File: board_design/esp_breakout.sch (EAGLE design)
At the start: 14 parts, among them J3 USB_MINI-B_SMT

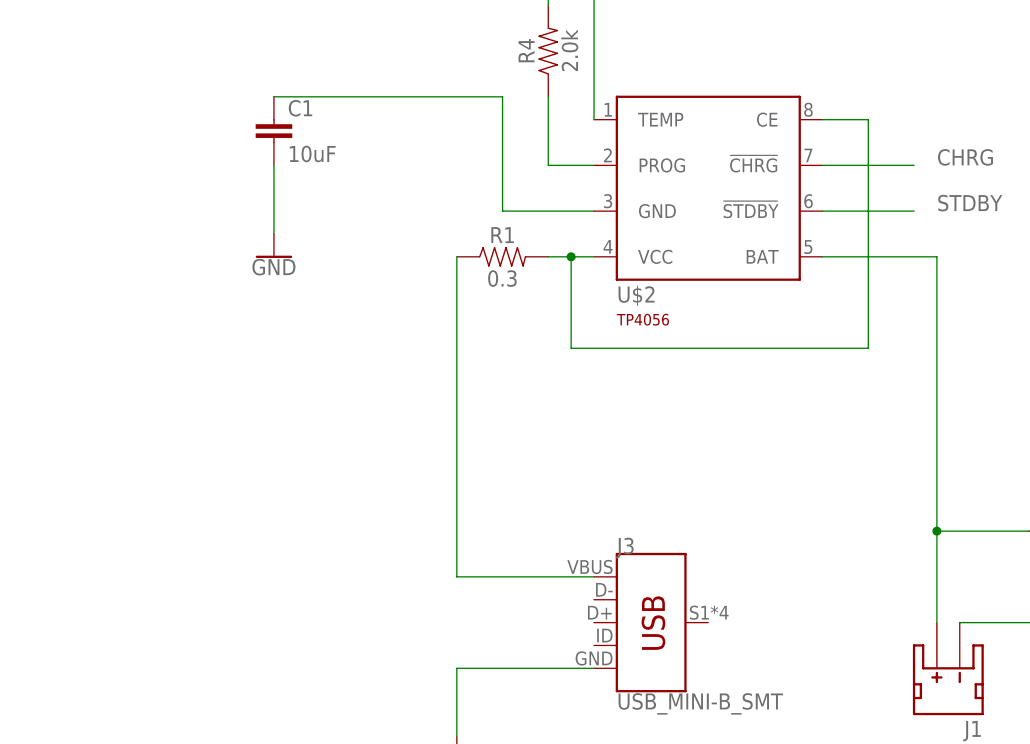
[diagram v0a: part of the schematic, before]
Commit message: upaded board to include 3.3v stepdown
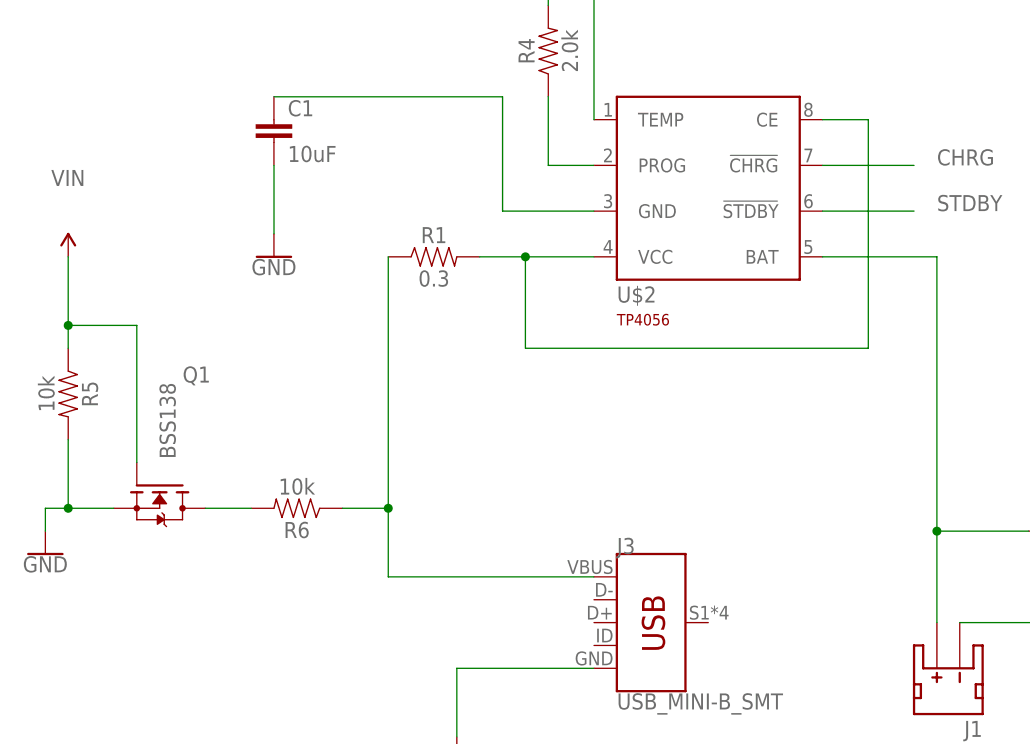
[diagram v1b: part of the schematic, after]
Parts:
- added Q1: BSS138, bss138_10:BSS138
- added R5, R6: 10k, SparkFun-Resistors:10KOHM-0603-1/10W-1%
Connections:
- new net N$10: Q1.D, R6.2
- net GND: now also Q1.S, R5.2
- net N$2: now also R6.1
- net VIN: now also Q1.G, R5.1
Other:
- moved on the sheet: R1
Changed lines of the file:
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@@
 <part name="C2" library="SparkFun-Capacitors" library_urn="urn:adsk.eagle:library:510" deviceset="10UF" device="-0805-10V-10%" package3d_urn="urn:adsk.eagle:package:37429/1" value="10uF"/>
 <part name="GND9" library="SparkFun-PowerSymbols" library_urn="urn:adsk.eagle:library:530" deviceset="GND" device=""/>
+<part name="Q1" library="bss138_10" deviceset="BSS138" device=""/>
+<part name="R6" library="SparkFun-Resistors" library_urn="urn:adsk.eagle:library:532" deviceset="10KOHM" device="-0603-1/10W-1%" package3d_urn="urn:adsk.eagle:package:39650/1" value="10k"/>
+<part name="R5" library="SparkFun-Resistors" library_urn="urn:adsk.eagle:library:532" deviceset="10KOHM" device="-0603-1/10W-1%" package3d_urn="urn:adsk.eagle:package:39650/1" value="10k"/>
+<part name="SUPPLY4" library="SparkFun-PowerSymbols" library_urn="urn:adsk.eagle:library:530" deviceset="VIN" device=""/>
+<part name="GND10" library="SparkFun-PowerSymbols" library_urn="urn:adsk.eagle:library:530" deviceset="GND" device=""/>
 </parts>
 <sheets>
@@
 <attribute name="NAME" x="-55.88" y="-48.26" size="1.778" layer="95" font="vector"/>
 </instance>
-<instance part="R1" gate="G$1" x="-68.58" y="-15.24" smashed="yes">
-<attribute name="NAME" x="-68.58" y="-13.716" size="1.778" layer="95" font="vector" align="bottom-center"/>
-<attribute name="VALUE" x="-68.58" y="-16.764" size="1.778" layer="96" font="vector" align="top-center"/>
+<instance part="R1" gate="G$1" x="-76.2" y="-15.24" smashed="yes">
+<attribute name="NAME" x="-76.2" y="-13.716" size="1.778" layer="95" font="vector" align="bottom-center"/>
+<attribute name="VALUE" x="-76.2" y="-16.764" size="1.778" layer="96" font="vector" align="top-center"/>
 </instance>
 <instance part="GND7" gate="1" x="-93.98" y="-15.24" smashed="yes">
@@
 <instance part="GND9" gate="1" x="7.62" y="-66.04" smashed="yes">
 <attribute name="VALUE" x="7.62" y="-66.294" size="1.778" layer="96" align="top-center"/>
+</instance>
+<instance part="Q1" gate="G$1" x="-106.68" y="-40.64" smashed="yes" rot="R270">
+<attribute name="VALUE" x="-106.68" y="-29.21" size="1.778" layer="96" rot="R270"/>
+<attribute name="NAME" x="-104.14" y="-29.21" size="1.778" layer="95"/>
+</instance>
+<instance part="R6" gate="G$1" x="-91.44" y="-43.18" smashed="yes" rot="R180">
+<attribute name="NAME" x="-91.44" y="-44.704" size="1.778" layer="95" font="vector" rot="R180" align="bottom-center"/>
+<attribute name="VALUE" x="-91.44" y="-41.656" size="1.778" layer="96" font="vector" rot="R180" align="top-center"/>
+</instance>
+<instance part="R5" gate="G$1" x="-116.84" y="-30.48" smashed="yes" rot="R270">
+<attribute name="NAME" x="-115.316" y="-30.48" size="1.778" layer="95" font="vector" rot="R270" align="bottom-center"/>
+<attribute name="VALUE" x="-118.364" y="-30.48" size="1.778" layer="96" font="vector" rot="R270" align="top-center"/>
+</instance>
+<instance part="SUPPLY4" gate="G$1" x="-116.84" y="-15.24" smashed="yes">
+<attribute name="VALUE" x="-116.84" y="-7.366" size="1.778" layer="96" align="bottom-center"/>
+</instance>
+<instance part="GND10" gate="1" x="-119.38" y="-48.26" smashed="yes">
+<attribute name="VALUE" x="-119.38" y="-48.514" size="1.778" layer="96" align="top-center"/>
 </instance>
 </instances>
@@
 <junction x="7.62" y="-55.88"/>
 </segment>
+<segment>
+<pinref part="Q1" gate="G$1" pin="S"/>
+<wire x1="-111.76" y1="-43.18" x2="-116.84" y2="-43.18" width="0.1524" layer="91"/>
+<pinref part="GND10" gate="1" pin="GND"/>
+<wire x1="-116.84" y1="-43.18" x2="-119.38" y2="-43.18" width="0.1524" layer="91"/>
+<wire x1="-119.38" y1="-43.18" x2="-119.38" y2="-45.72" width="0.1524" layer="91"/>
+<pinref part="R5" gate="G$1" pin="2"/>
+<wire x1="-116.84" y1="-35.56" x2="-116.84" y2="-43.18" width="0.1524" layer="91"/>
+<junction x="-116.84" y="-43.18"/>
+</segment>
 </net>
 <net name="N$1" class="0">
@@
 <pinref part="SUPPLY2" gate="G$1" pin="VIN"/>
 </segment>
+<segment>
+<pinref part="Q1" gate="G$1" pin="G"/>
+<wire x1="-109.22" y1="-38.1" x2="-109.22" y2="-22.86" width="0.1524" layer="91"/>
+<wire x1="-109.22" y1="-22.86" x2="-116.84" y2="-22.86" width="0.1524" layer="91"/>
+<pinref part="R5" gate="G$1" pin="1"/>
+<wire x1="-116.84" y1="-22.86" x2="-116.84" y2="-25.4" width="0.1524" layer="91"/>
+<pinref part="SUPPLY4" gate="G$1" pin="VIN"/>
+<wire x1="-116.84" y1="-15.24" x2="-116.84" y2="-22.86" width="0.1524" layer="91"/>
+<junction x="-116.84" y="-22.86"/>
+</segment>
 </net>
 <net name="N$2" class="0">
@@
 <pinref part="R1" gate="G$1" pin="1"/>
 <pinref part="J3" gate="G$1" pin="VBUS"/>
-<wire x1="-73.66" y1="-15.24" x2="-73.66" y2="-50.8" width="0.1524" layer="91"/>
-<wire x1="-73.66" y1="-50.8" x2="-58.42" y2="-50.8" width="0.1524" layer="91"/>
+<wire x1="-81.28" y1="-15.24" x2="-81.28" y2="-43.18" width="0.1524" layer="91"/>
+<wire x1="-81.28" y1="-43.18" x2="-81.28" y2="-50.8" width="0.1524" layer="91"/>
+<wire x1="-81.28" y1="-50.8" x2="-58.42" y2="-50.8" width="0.1524" layer="91"/>
+<pinref part="R6" gate="G$1" pin="1"/>
+<wire x1="-86.36" y1="-43.18" x2="-81.28" y2="-43.18" width="0.1524" layer="91"/>
+<junction x="-81.28" y="-43.18"/>
 </segment>
 </net>
@@
 <pinref part="U$2" gate="G$1" pin="VCC"/>
 <pinref part="R1" gate="G$1" pin="2"/>
-<wire x1="-58.42" y1="-15.24" x2="-60.96" y2="-15.24" width="0.1524" layer="91"/>
 <pinref part="U$2" gate="G$1" pin="CE"/>
-<wire x1="-60.96" y1="-15.24" x2="-63.5" y2="-15.24" width="0.1524" layer="91"/>
+<wire x1="-58.42" y1="-15.24" x2="-66.04" y2="-15.24" width="0.1524" layer="91"/>
+<wire x1="-66.04" y1="-15.24" x2="-71.12" y2="-15.24" width="0.1524" layer="91"/>
 <wire x1="-33.02" y1="0" x2="-27.94" y2="0" width="0.1524" layer="91"/>
 <wire x1="-27.94" y1="0" x2="-27.94" y2="-25.4" width="0.1524" layer="91"/>
-<wire x1="-27.94" y1="-25.4" x2="-60.96" y2="-25.4" width="0.1524" layer="91"/>
-<wire x1="-60.96" y1="-25.4" x2="-60.96" y2="-15.24" width="0.1524" layer="91"/>
-<junction x="-60.96" y="-15.24"/>
+<wire x1="-27.94" y1="-25.4" x2="-66.04" y2="-25.4" width="0.1524" layer="91"/>
+<wire x1="-66.04" y1="-25.4" x2="-66.04" y2="-15.24" width="0.1524" layer="91"/>
+<junction x="-66.04" y="-15.24"/>
 </segment>
 </net>
@@
 </segment>
 </net>
+<net name="N$10" class="0">
+<segment>
+<pinref part="Q1" gate="G$1" pin="D"/>
+<pinref part="R6" gate="G$1" pin="2"/>
+<wire x1="-101.6" y1="-43.18" x2="-96.52" y2="-43.18" width="0.1524" layer="91"/>
+</segment>
+</net>
